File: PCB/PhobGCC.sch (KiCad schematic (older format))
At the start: 43 parts, among them J1 Conn_01x06_Female, J2 Conn_01x04_Female, J3 Conn_01x01_Male, J4 Conn_01x01_Male, J6 10118194-0001LF, SW1 A, SW10 Dup, SW11 Dright, SW12 Ddown, SW2 B, SW3 X, SW4 Y, SW5 Start, SW6 L, SW7 R, SW8 1825027-5, SW9 Dleft, U1 Teensy3.2, U2 Stickbox_Assembly

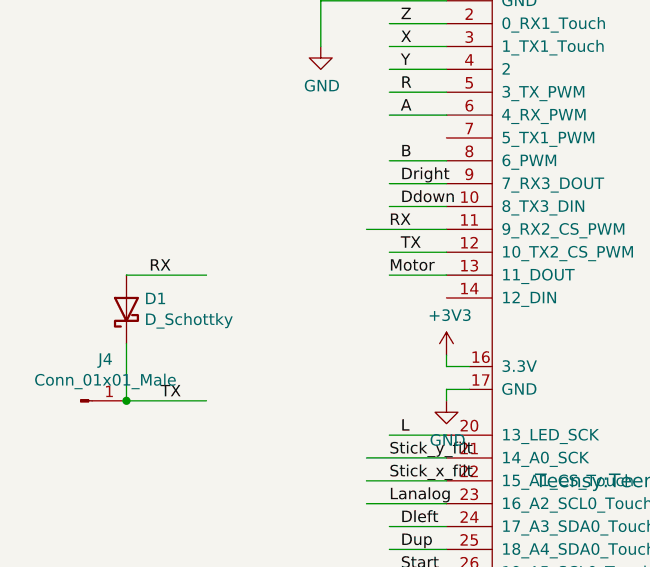
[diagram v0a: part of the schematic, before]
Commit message: Changed schematic so that it "should" work with a teensy 3.2 or 4.0. Will require the pins of 2 of the d-pad buttons to be updated in the software.
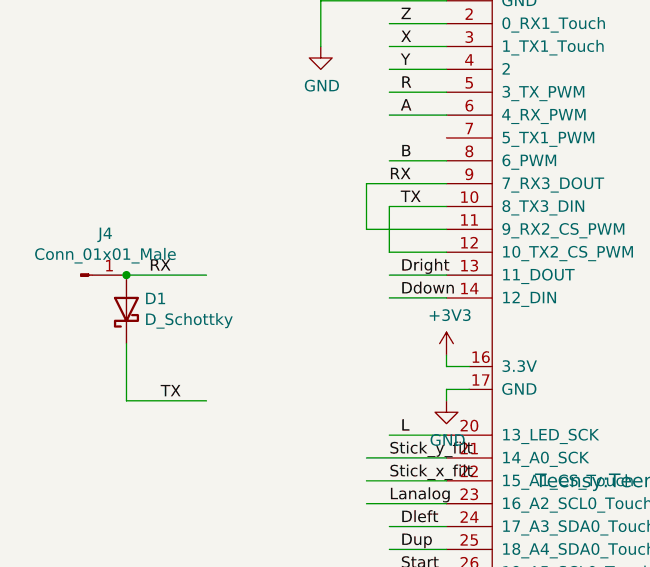
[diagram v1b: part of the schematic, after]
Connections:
- net labels removed: Motor
- wire segments 145 -> 148
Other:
- moved on the sheet: J4
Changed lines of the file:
@@
 	2200 5000 1950 5000
 Wire Wire Line
-	2200 3400 1950 3400
-Wire Wire Line
-	2200 3500 1950 3500
+	2200 3800 1950 3800
+Wire Wire Line
+	2200 3900 1950 3900
 Text Label 2000 4900 0    50   ~ 0
 Dleft
 Text Label 2000 5000 0    50   ~ 0
 Dup
-Text Label 2000 3400 0    50   ~ 0
+Text Label 2000 3800 0    50   ~ 0
 Dright
-Text Label 2000 3500 0    50   ~ 0
+Text Label 2000 3900 0    50   ~ 0
 Ddown
 $Comp
@@
 Text Label 1950 4700 0    50   ~ 0
 Stick_x_filt
-Text Label 1950 3600 0    50   ~ 0
+Text Label 1950 3400 0    50   ~ 0
 RX
-Text Label 1950 3800 0    50   ~ 0
-Motor
-Wire Wire Line
-	2200 3800 1950 3800
 $Comp
 L Connector:Conn_01x01_Male J4
 U 1 1 61CB4987
-P 600 4350
-F 0 "J4" H 708 4531 50  0000 C CNN
-F 1 "Conn_01x01_Male" H 708 4440 50  0000 C CNN
-F 2 "Connector_PinHeader_2.54mm:PinHeader_1x01_P2.54mm_Vertical" H 600 4350 50  0001 C CNN
-F 3 "~" H 600 4350 50  0001 C CNN
-	1    600  4350
+P 600 3800
+F 0 "J4" H 708 3981 50  0000 C CNN
+F 1 "Conn_01x01_Male" H 708 3890 50  0000 C CNN
+F 2 "Connector_PinHeader_2.54mm:PinHeader_1x01_P2.54mm_Vertical" H 600 3800 50  0001 C CNN
+F 3 "~" H 600 3800 50  0001 C CNN
+	1    600  3800
 	1    0    0    -1
 $EndComp
@@
 D+
 Wire Wire Line
-	2200 3600 1850 3600
-Text Label 2000 3700 0    50   ~ 0
+	2200 3400 1850 3400
+Text Label 2000 3500 0    50   ~ 0
 TX
 Wire Wire Line
-	2200 3700 1950 3700
+	2200 3500 1950 3500
 Wire Wire Line
 	800  4100 800  4350
 Wire Wire Line
 	800  4350 1150 4350
-Connection ~ 800  4350
 Wire Wire Line
 	800  3800 1150 3800
@@
 Text Label 1000 6650 0    50   ~ 0
 Stick_x
+Wire Wire Line
+	1950 3500 1950 3700
+Wire Wire Line
+	1950 3700 2200 3700
+Wire Wire Line
+	1850 3400 1850 3600
+Wire Wire Line
+	1850 3600 2200 3600
+Connection ~ 800  3800
 $EndSCHEMATC

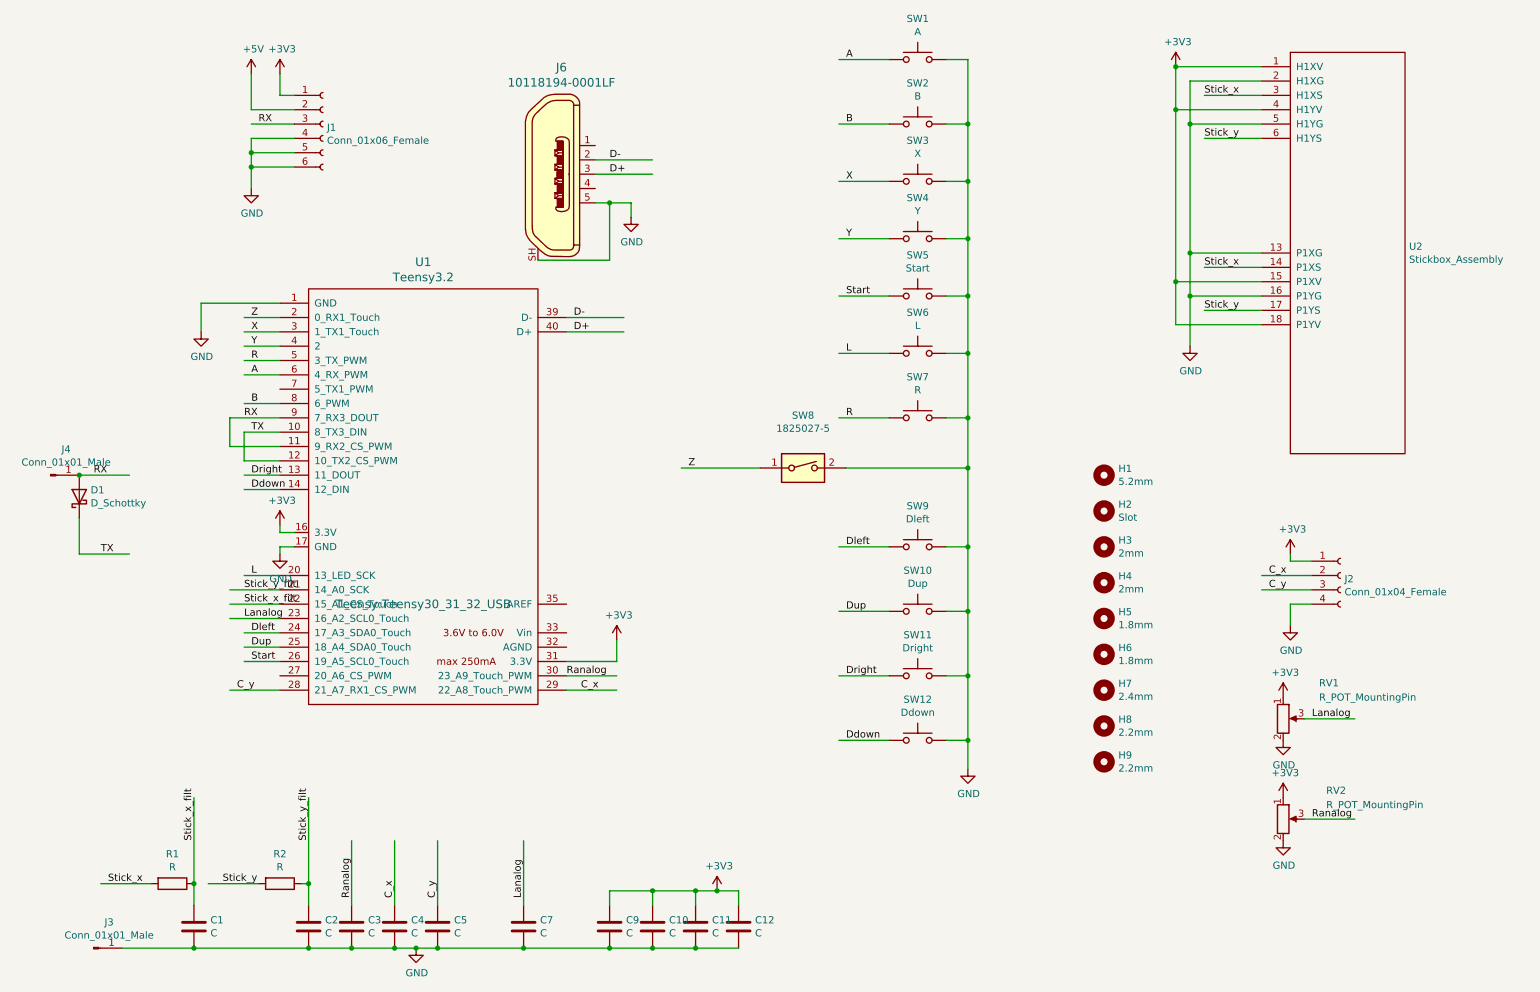
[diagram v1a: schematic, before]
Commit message: Added electronics BOM and put values in schematic
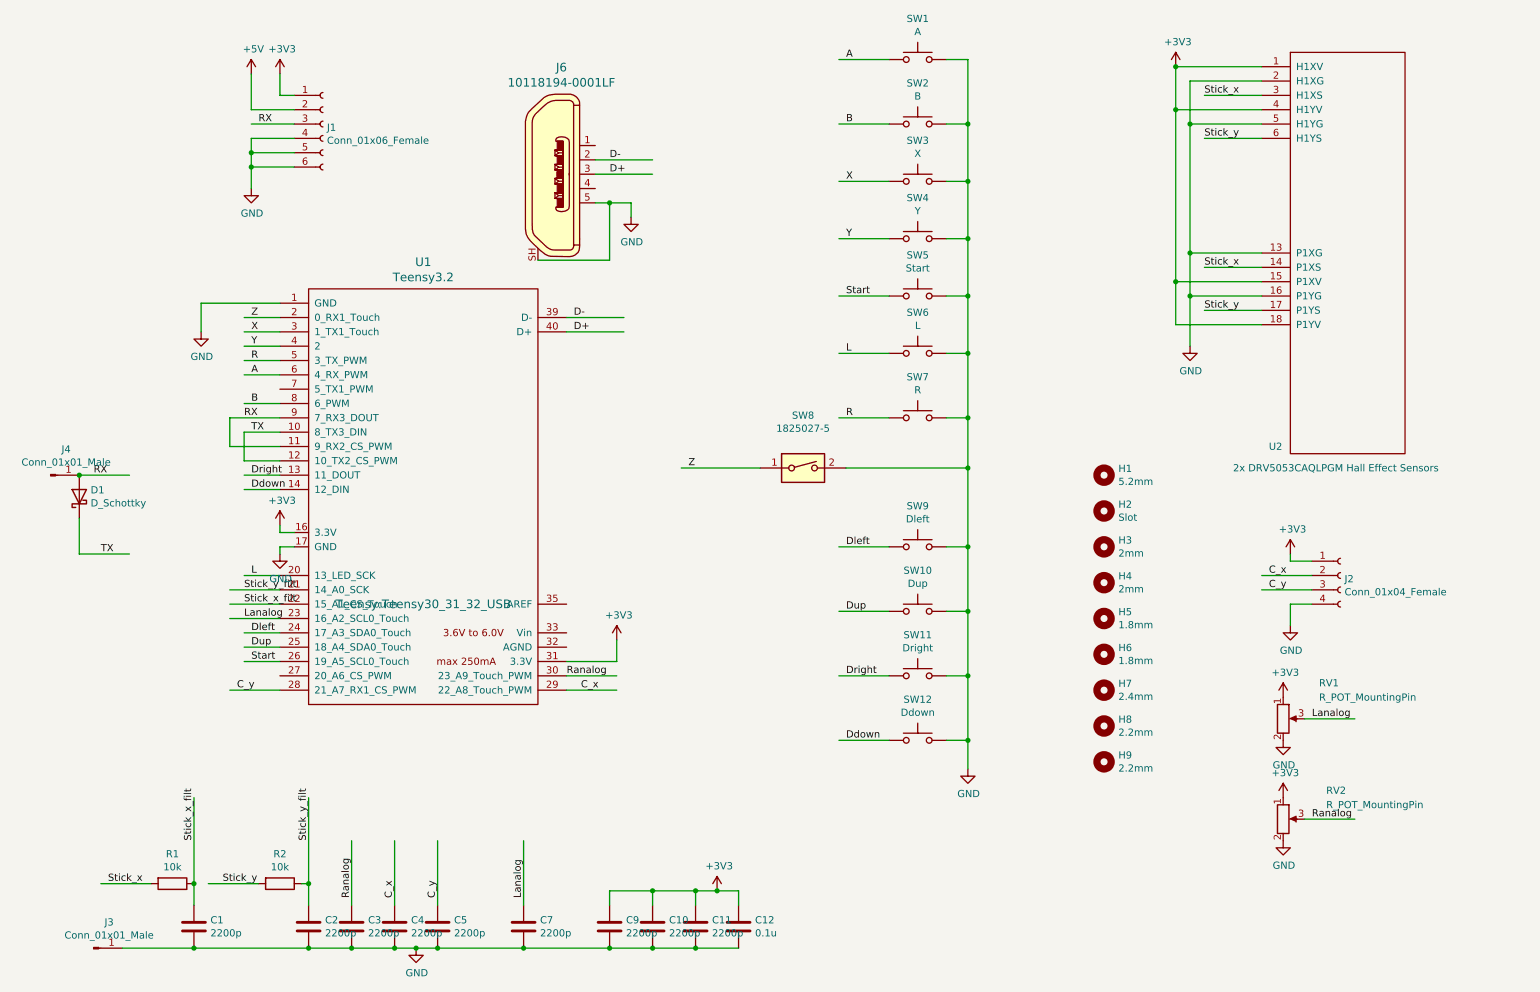
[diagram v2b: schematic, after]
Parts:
- C1, C10, C11, C2, C3, C4, C5, C7, C9: value C -> 2200p
- C12: value C -> 0.1u
- R1, R2: value R -> 10k
- U2: value Stickbox_Assembly -> 2x DRV5053CAQLPGM Hall Effect Sensors
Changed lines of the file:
@@
 P 2400 6950
 F 0 "C2" H 2515 6996 50  0000 L CNN
-F 1 "C" H 2515 6905 50  0000 L CNN
+F 1 "2200p" H 2515 6905 50  0000 L CNN
 F 2 "Capacitors_SMD:C_0603_HandSoldering" H 2438 6800 50  0001 C CNN
 F 3 "~" H 2400 6950 50  0001 C CNN
@@
 P 2700 6950
 F 0 "C3" H 2815 6996 50  0000 L CNN
-F 1 "C" H 2815 6905 50  0000 L CNN
+F 1 "2200p" H 2815 6905 50  0000 L CNN
 F 2 "Capacitors_SMD:C_0603_HandSoldering" H 2738 6800 50  0001 C CNN
 F 3 "~" H 2700 6950 50  0001 C CNN
@@
 P 3000 6950
 F 0 "C4" H 3115 6996 50  0000 L CNN
-F 1 "C" H 3115 6905 50  0000 L CNN
+F 1 "2200p" H 3115 6905 50  0000 L CNN
 F 2 "Capacitors_SMD:C_0603_HandSoldering" H 3038 6800 50  0001 C CNN
 F 3 "~" H 3000 6950 50  0001 C CNN
@@
 P 3300 6950
 F 0 "C5" H 3415 6996 50  0000 L CNN
-F 1 "C" H 3415 6905 50  0000 L CNN
+F 1 "2200p" H 3415 6905 50  0000 L CNN
 F 2 "Capacitors_SMD:C_0603_HandSoldering" H 3338 6800 50  0001 C CNN
 F 3 "~" H 3300 6950 50  0001 C CNN
@@
 P 3900 6950
 F 0 "C7" H 4015 6996 50  0000 L CNN
-F 1 "C" H 4015 6905 50  0000 L CNN
+F 1 "2200p" H 4015 6905 50  0000 L CNN
 F 2 "Capacitors_SMD:C_0603_HandSoldering" H 3938 6800 50  0001 C CNN
 F 3 "~" H 3900 6950 50  0001 C CNN
@@
 P 4800 6950
 F 0 "C10" H 4915 6996 50  0000 L CNN
-F 1 "C" H 4915 6905 50  0000 L CNN
+F 1 "2200p" H 4915 6905 50  0000 L CNN
 F 2 "Capacitors_SMD:C_0603_HandSoldering" H 4838 6800 50  0001 C CNN
 F 3 "~" H 4800 6950 50  0001 C CNN
@@
 P 4500 6950
 F 0 "C9" H 4615 6996 50  0000 L CNN
-F 1 "C" H 4615 6905 50  0000 L CNN
+F 1 "2200p" H 4615 6905 50  0000 L CNN
 F 2 "Capacitors_SMD:C_0603_HandSoldering" H 4538 6800 50  0001 C CNN
 F 3 "~" H 4500 6950 50  0001 C CNN
@@
 P 5100 6950
 F 0 "C11" H 5215 6996 50  0000 L CNN
-F 1 "C" H 5215 6905 50  0000 L CNN
+F 1 "2200p" H 5215 6905 50  0000 L CNN
 F 2 "Capacitors_SMD:C_0603_HandSoldering" H 5138 6800 50  0001 C CNN
 F 3 "~" H 5100 6950 50  0001 C CNN
@@
 P 5400 6950
 F 0 "C12" H 5515 6996 50  0000 L CNN
-F 1 "C" H 5515 6905 50  0000 L CNN
+F 1 "0.1u" H 5515 6905 50  0000 L CNN
 F 2 "Capacitors_SMD:C_0603_HandSoldering" H 5438 6800 50  0001 C CNN
 F 3 "~" H 5400 6950 50  0001 C CNN
@@
 U 1 1 615AFD68
 P 9250 850
-F 0 "U2" H 10078 -504 50  0000 L CNN
-F 1 "Stickbox_Assembly" H 10078 -595 50  0000 L CNN
+F 0 "U2" H 9100 -1900 50  0000 L CNN
+F 1 "2x DRV5053CAQLPGM Hall Effect Sensors" H 8850 -2050 50  0000 L CNN
 F 2 "Gamecube MB:GCC_Stickbox_2" H 9250 -450 50  0001 C CNN
 F 3 "" H 9250 -450 50  0001 C CNN
@@
 P 1600 6950
 F 0 "C1" H 1715 6996 50  0000 L CNN
-F 1 "C" H 1715 6905 50  0000 L CNN
+F 1 "2200p" H 1715 6905 50  0000 L CNN
 F 2 "Capacitors_SMD:C_0603_HandSoldering" H 1638 6800 50  0001 C CNN
 F 3 "~" H 1600 6950 50  0001 C CNN
@@
 P 1450 6650
 F 0 "R1" V 1243 6650 50  0000 C CNN
-F 1 "R" V 1334 6650 50  0000 C CNN
+F 1 "10k" V 1334 6650 50  0000 C CNN
 F 2 "Resistor_SMD:R_0603_1608Metric" V 1380 6650 50  0001 C CNN
 F 3 "~" H 1450 6650 50  0001 C CNN
@@
 P 2200 6650
 F 0 "R2" V 1993 6650 50  0000 C CNN
-F 1 "R" V 2084 6650 50  0000 C CNN
+F 1 "10k" V 2084 6650 50  0000 C CNN
 F 2 "Resistor_SMD:R_0603_1608Metric" V 2130 6650 50  0001 C CNN
 F 3 "~" H 2200 6650 50  0001 C CNN

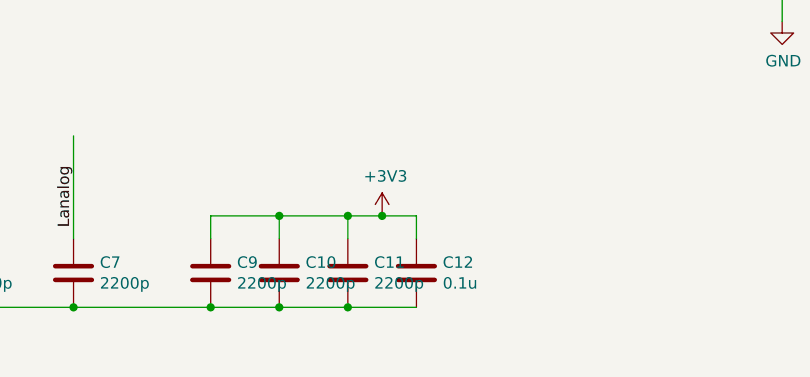
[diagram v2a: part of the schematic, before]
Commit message: cap value assignment was wrong, fixed
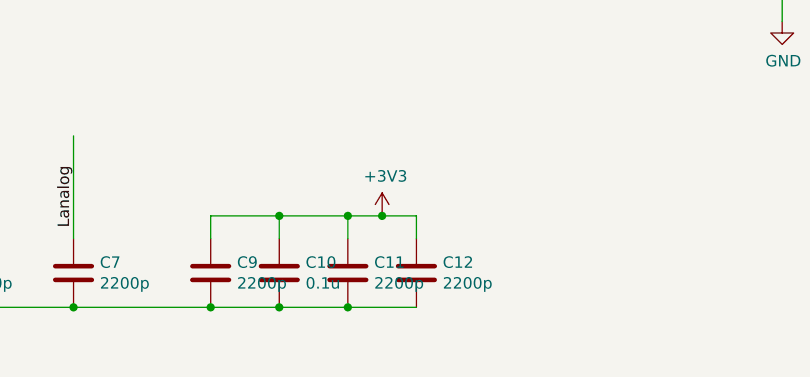
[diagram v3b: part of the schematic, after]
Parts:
- C10: value 2200p -> 0.1u
- C12: value 0.1u -> 2200p
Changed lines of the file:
@@
 P 4800 6950
 F 0 "C10" H 4915 6996 50  0000 L CNN
-F 1 "2200p" H 4915 6905 50  0000 L CNN
+F 1 "0.1u" H 4915 6905 50  0000 L CNN
 F 2 "Capacitors_SMD:C_0603_HandSoldering" H 4838 6800 50  0001 C CNN
 F 3 "~" H 4800 6950 50  0001 C CNN
@@
 P 5400 6950
 F 0 "C12" H 5515 6996 50  0000 L CNN
-F 1 "0.1u" H 5515 6905 50  0000 L CNN
+F 1 "2200p" H 5515 6905 50  0000 L CNN
 F 2 "Capacitors_SMD:C_0603_HandSoldering" H 5438 6800 50  0001 C CNN
 F 3 "~" H 5400 6950 50  0001 C CNN

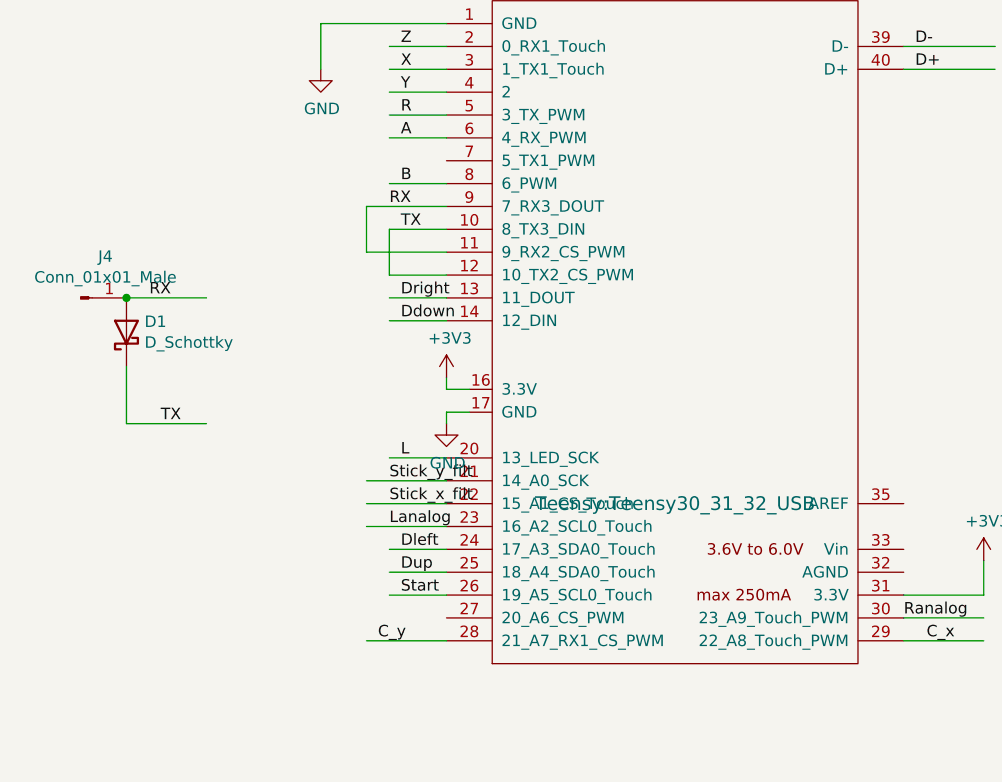
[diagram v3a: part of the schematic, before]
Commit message: Updated layout so the LED pin doesn't get used, added link to wiki in readme.
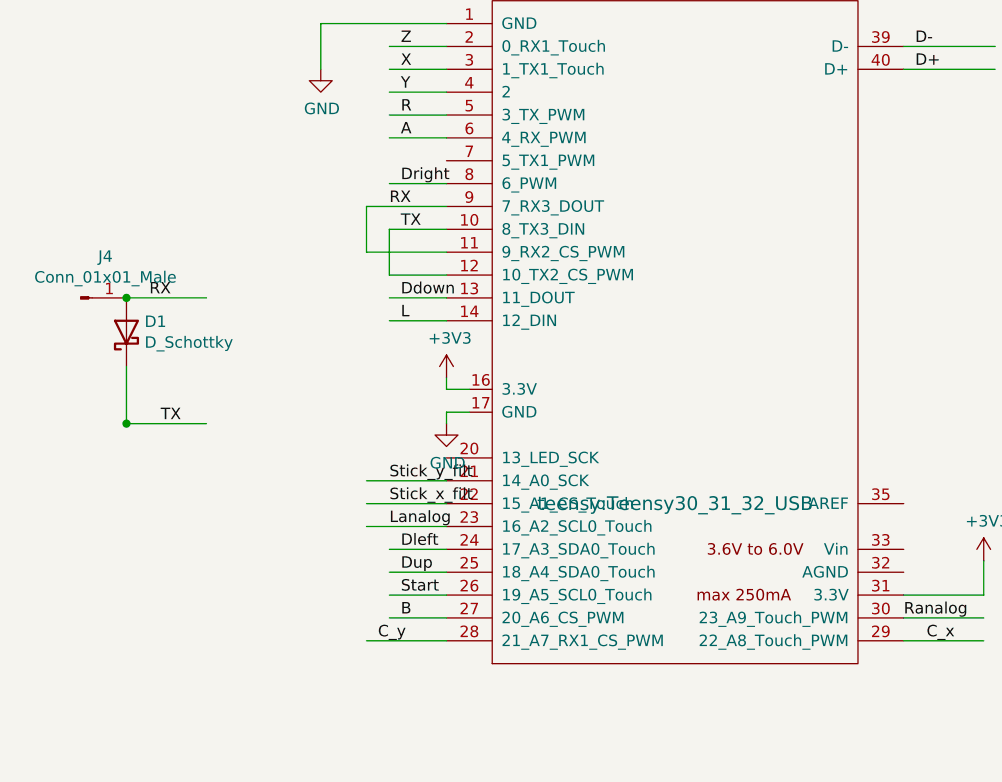
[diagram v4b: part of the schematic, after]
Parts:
- D1: footprint Diode_SMD:D_SOD-523 -> Gamecube MB:D_SOD-523_large_pads
- U1: footprint Teensy:Teensy30_31_32_USB -> teensy:Teensy30_31_32_USB
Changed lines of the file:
@@
 Z
 Wire Wire Line
-	2200 3300 1950 3300
+	2200 5200 1950 5200
 Wire Wire Line
 	2200 2900 1950 2900
@@
 	2200 5100 1950 5100
 Wire Wire Line
-	2200 4500 1950 4500
+	2200 3900 1950 3900
 Wire Wire Line
 	2200 3000 1950 3000
 Text Label 2000 3100 0    50   ~ 0
 A
-Text Label 2000 3300 0    50   ~ 0
+Text Label 2000 5200 0    50   ~ 0
 B
 Text Label 2000 2800 0    50   ~ 0
@@
 	2200 5000 1950 5000
 Wire Wire Line
+	2200 3300 1950 3300
+Wire Wire Line
 	2200 3800 1950 3800
-Wire Wire Line
-	2200 3900 1950 3900
 Text Label 2000 4900 0    50   ~ 0
 Dleft
 Text Label 2000 5000 0    50   ~ 0
 Dup
+Text Label 2000 3300 0    50   ~ 0
+Dright
 Text Label 2000 3800 0    50   ~ 0
-Dright
-Text Label 2000 3900 0    50   ~ 0
 Ddown
 $Comp
@@
 F 0 "U1" H 3200 5587 60  0000 C CNN
 F 1 "Teensy3.2" H 3200 5481 60  0000 C CNN
-F 2 "Teensy:Teensy30_31_32_USB" H 3200 3200 60  0000 C CNN
+F 2 "teensy:Teensy30_31_32_USB" H 3200 3200 60  0000 C CNN
 F 3 "" H 3200 3200 60  0000 C CNN
 	1    3200 3950
@@
 	1    0    0    -1
 $EndComp
-Text Label 2000 4500 0    50   ~ 0
+Text Label 2000 3900 0    50   ~ 0
 L
-$Comp
-L Device:D_Schottky D1
-U 1 1 61C761F4
-P 800 3950
-F 0 "D1" V 846 3871 50  0000 R CNN
-F 1 "D_Schottky" V 755 3871 50  0000 R CNN
-F 2 "Diode_SMD:D_SOD-523" H 800 3950 50  0001 C CNN
-F 3 "~" H 800 3950 50  0001 C CNN
-	1    800  3950
-	0    -1   -1   0
-$EndComp
 Text Label 1950 4700 0    50   ~ 0
 Stick_x_filt
@@
 Wire Wire Line
 	1850 3600 2200 3600
+Connection ~ 800  4350
+$Comp
+L Device:D_Schottky D1
+U 1 1 61C761F4
+P 800 3950
+F 0 "D1" V 846 3871 50  0000 R CNN
+F 1 "D_Schottky" V 755 3871 50  0000 R CNN
+F 2 "Gamecube MB:D_SOD-523_large_pads" H 800 3950 50  0001 C CNN
+F 3 "~" H 800 3950 50  0001 C CNN
+	1    800  3950
+	0    -1   -1   0
+$EndComp
 Connection ~ 800  3800
 $EndSCHEMATC
